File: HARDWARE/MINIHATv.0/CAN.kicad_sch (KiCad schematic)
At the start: 0 parts

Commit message: CAN schematic circuit added
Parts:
- added C3, C8: 100n, symbol Device:C
- added C4: 4n7, symbol Device:C
- added C5, C6: 30p, symbol Device:C
- added D3: TVS 14V, Package_TO_SOT_SMD:SOT-323_SC-70, symbol Power_Protection:SP0502BAJT
- added J2: Conn_01x04_Pin, symbol Connector:Conn_01x04_Pin
- added R11, R12: 60, symbol Device:R
- added R15: 4k7, symbol Device:R
- added SW1, SW2: SW_Nidec_CAS-120A1, Button_Switch_SMD:Nidec_Copal_CAS-120A, symbol Switch:SW_Nidec_CAS-120A1
- added U3: TCAN332, symbol Interface_CAN_LIN:TCAN332
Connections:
- new net: R12.1, SW1.1 (C)
- new net: C4.1, R11.1, R12.2
- new net: R11.2, SW2.3 (A)
- new net +3V3: C3.1, R15.1, U3.3 (VCC)
- new net CAN_H: C5.1, D3.1 (K), J2.3 (Pin_3), SW1.2 (B), U3.7 (CANH)
- new net CAN_L: C6.1, D3.2 (K), J2.2 (Pin_2), SW2.2 (B), U3.6 (CANL)
- new net FDCAN_Rx: U3.4 (RXD)
- new net FDCAN_Tx: C8.1, R15.2, U3.1 (TXD)
- new net GND: C3.2, C4.2, C5.2, C6.2, C8.2, D3.3 (A), U3.2 (GND)
- no-connect marks 0 -> 2
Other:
- note added: "miejsce lutowania taśmy z con.51115-1601 molex"

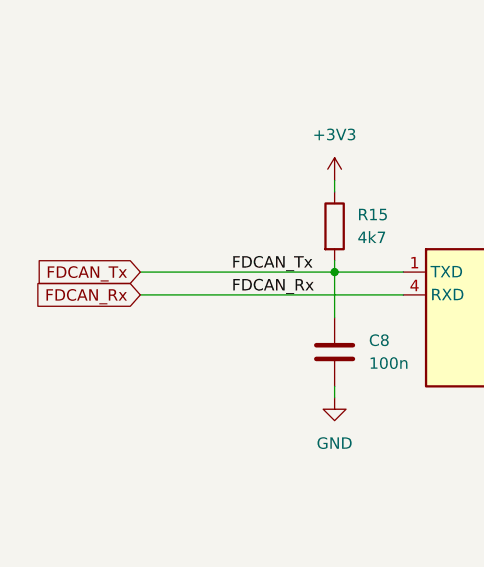
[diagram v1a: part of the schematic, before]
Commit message: added HDMI page
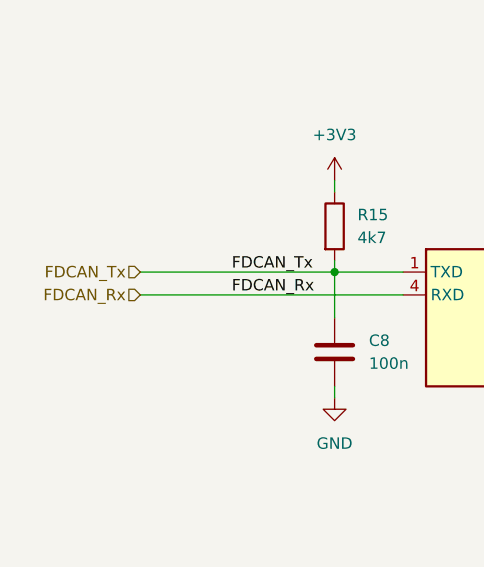
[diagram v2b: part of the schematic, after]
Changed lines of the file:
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@@
 		)
 	)
-	(global_label "FDCAN_Tx"
+	(hierarchical_label "FDCAN_Tx"
 		(shape input)
 		(at 67.31 87.63 180)
-		(fields_autoplaced yes)
 		(effects
 			(font
@@
 			(justify right)
 		)
-		(property "Intersheetrefs" "${INTERSHEET_REFS}"
-			(at 55.3138 87.63 0)
-			(hide yes)
-			(show_name no)
-			(do_not_autoplace no)
-			(effects
-				(font
-					(size 1.27 1.27)
-				)
-				(justify right)
-			)
-		)
 	)
-	(global_label "FDCAN_Rx"
+	(hierarchical_label "FDCAN_Rx"
 		(shape input)
 		(at 67.31 90.17 180)
-		(fields_autoplaced yes)
 		(effects
 			(font
@@
 			(justify right)
 		)
-		(property "Intersheetrefs" "${INTERSHEET_REFS}"
-			(at 55.0114 90.17 0)
-			(hide yes)
-			(show_name no)
-			(do_not_autoplace no)
-			(effects
-				(font
-					(size 1.27 1.27)
-				)
-				(justify right)
-			)
-		)
 	)

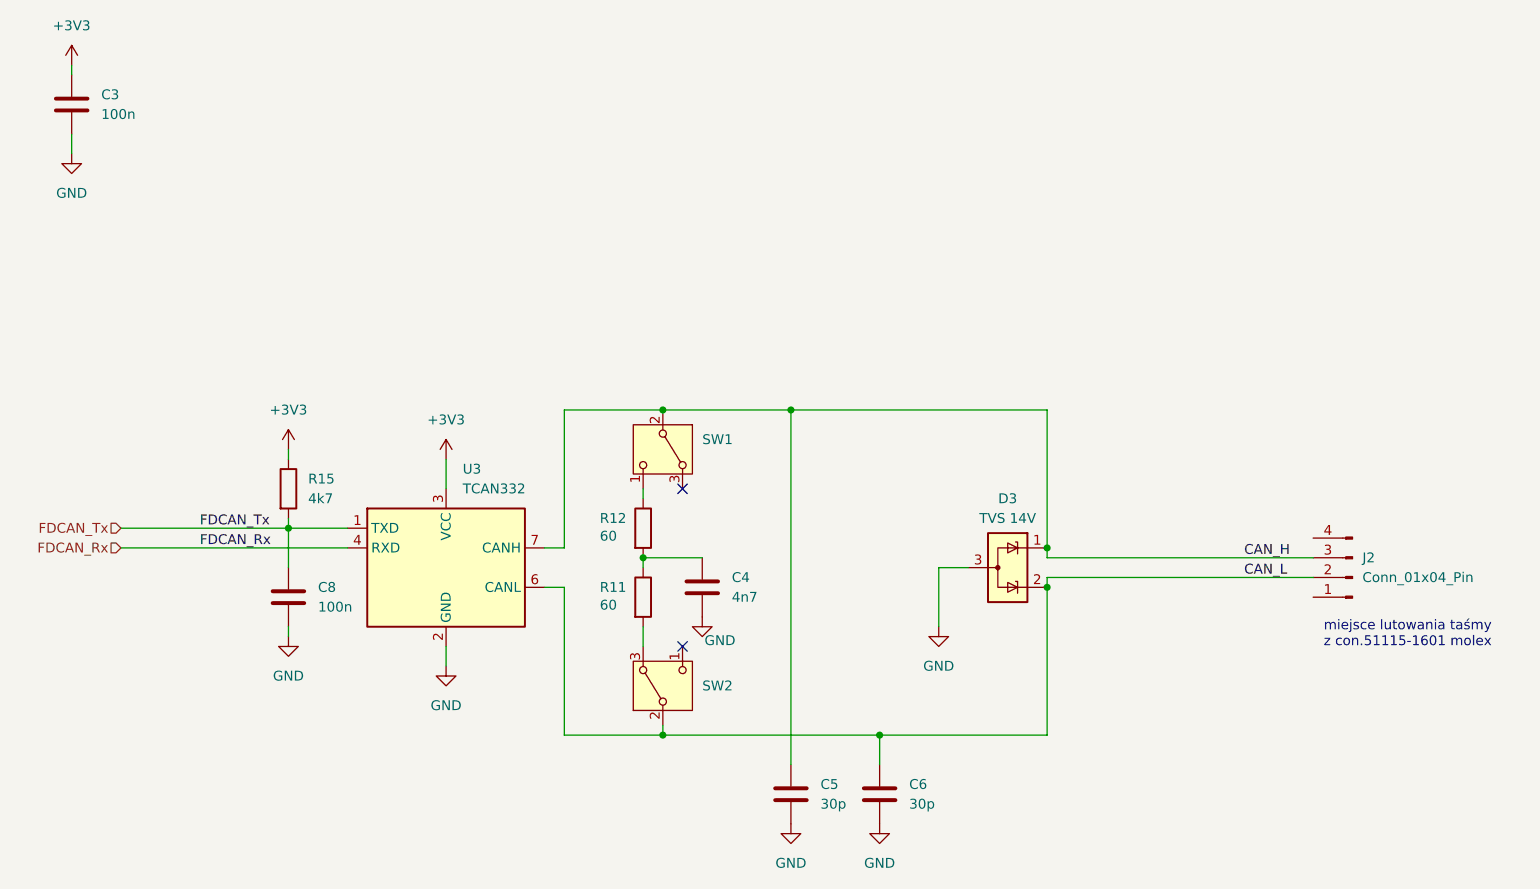
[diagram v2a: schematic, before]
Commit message: added i2c for hdmi
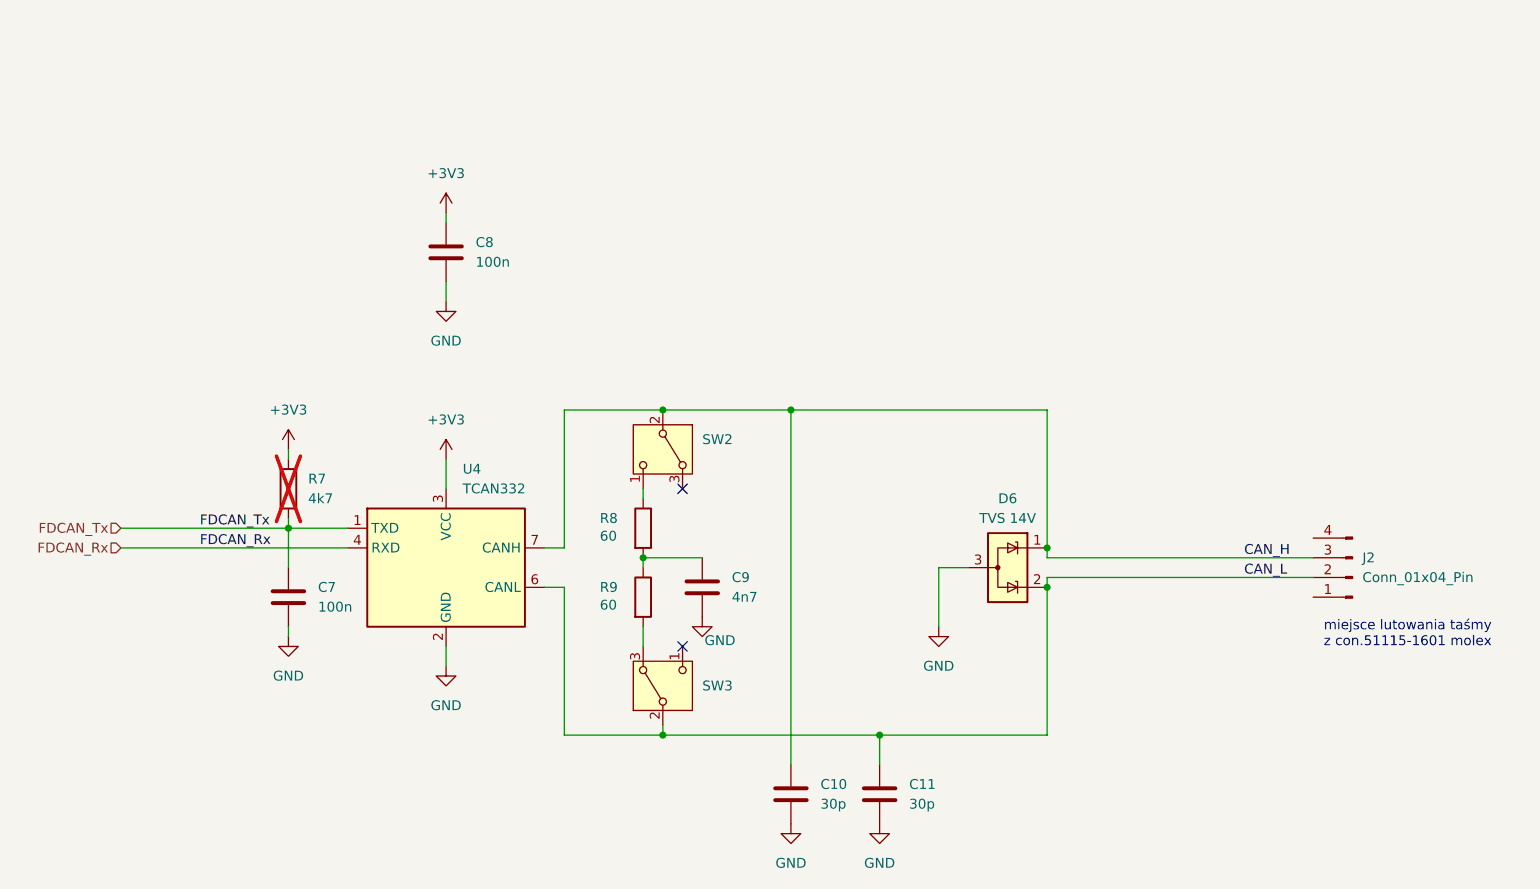
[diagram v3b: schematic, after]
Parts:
- R7: renamed from R15; now not fitted
- renumbered C5 to C10, C6 to C11, C8 to C7, C3 to C8, C4 to C9, D3 to D6, R12 to R8, R11 to R9, SW1 to SW2, SW2 to SW3, U3 to U4
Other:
- moved on the sheet: C8
